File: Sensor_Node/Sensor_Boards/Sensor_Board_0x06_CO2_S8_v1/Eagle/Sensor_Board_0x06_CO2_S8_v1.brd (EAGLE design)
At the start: 55 x 35 mm, 15 parts, among them J1 M04_SMD_90, J3 M03_SMD_90, J4 ARDUINO_ISP, U1 SENSEAIR_S8_SMD, U2 ATMEGA328P_TQFP, Y1 8MHZ

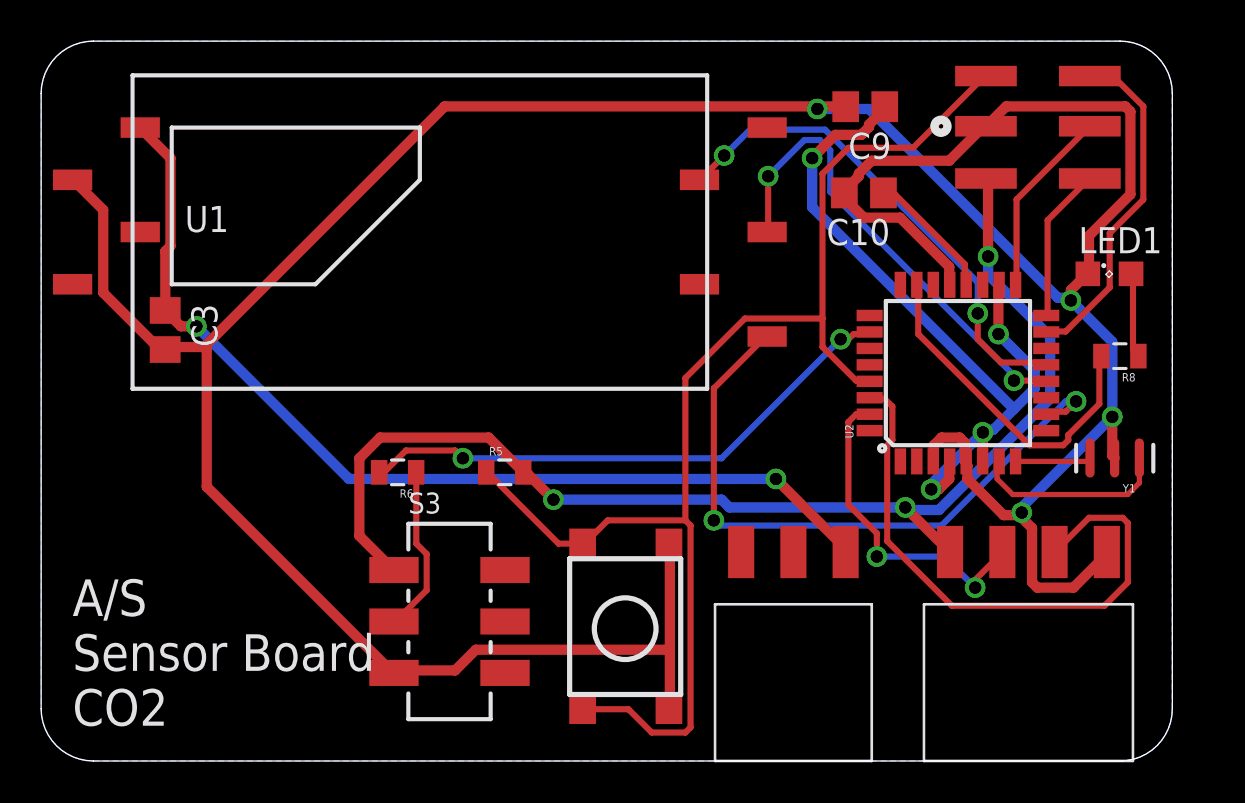
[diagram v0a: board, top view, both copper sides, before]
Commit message: Changes on SensModule CO2 S8
- added poppin programming connector
- moved communication connectors closer together
- turned C3
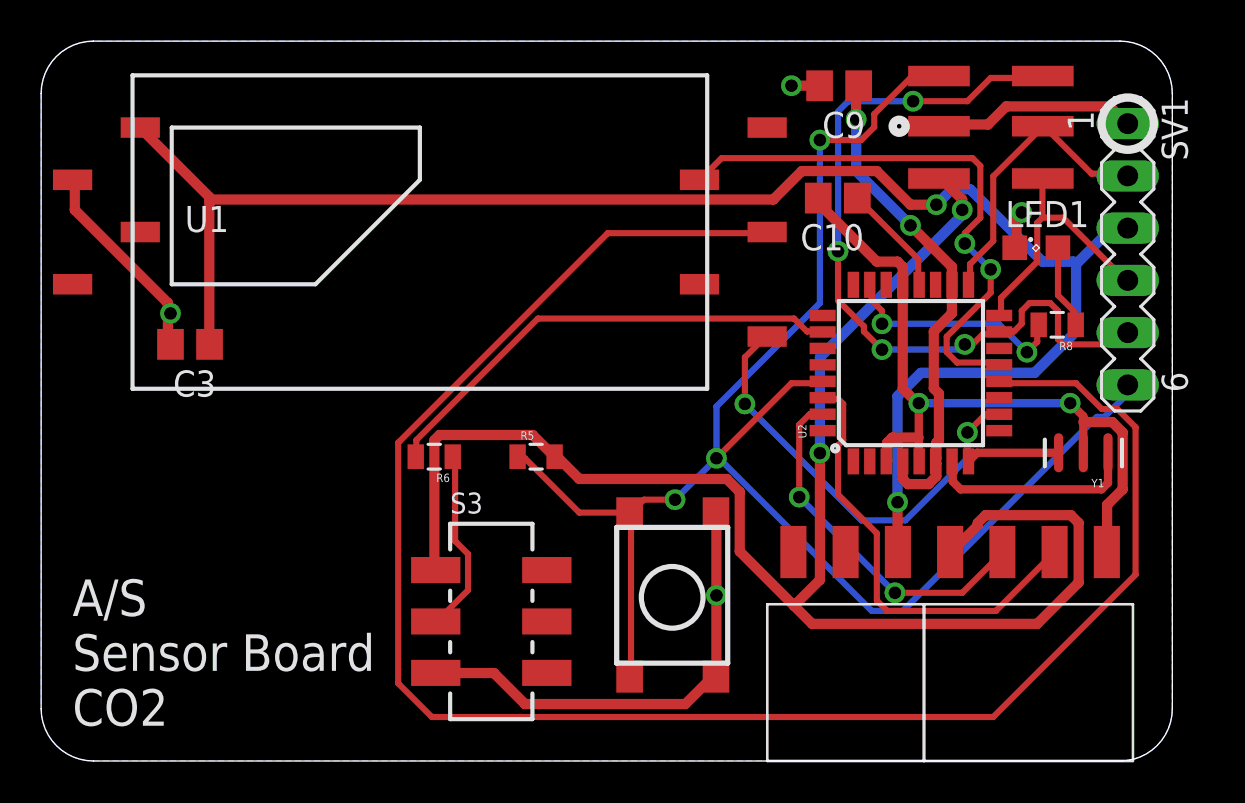
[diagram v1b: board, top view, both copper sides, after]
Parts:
- added SV1: (no value), con-lstb:MA06-1
- moved LED1 3.78 mm to (48.4, 25.0)
- moved R8 3.41 mm to (49.4, 21.2)
- moved S1 2.75 mm to (32.8, 12.0)
- moved J3 2.54 mm to (36.6, 10.2)
- moved U2 2.29 mm to (42.3, 18.9)
- moved J4 2.29 mm to (48.7, 28.3)
- moved S3 2.03 mm to (21.9, 6.78)
- moved R6 1.93 mm to (19.1, 14.8)
- moved R5 1.70 mm to (24.1, 14.8)
- moved C9 1.63 mm to (38.8, 32.8)
- moved Y1 1.55 mm to (50.7, 15.0)
- moved C3 1.39 mm to (7.24, 20.3), turned to 180 degrees
- moved C10 1.30 mm to (38.7, 27.4)
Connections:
- net +5V: now also SV1.3
- net GND: now also SV1.1
- net MISO: now also SV1.4
- net MOSI: now also SV1.5
- net RESET: now also SV1.6
- net SCK: now also SV1.2
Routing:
- net GND: track 170.9 -> 82.3 mm, vias 4 -> 6
- net SENS_TX: track 23.2 -> 88.0 mm, vias 2 -> 0
- net +5V: track 47.7 -> 81.2 mm
- net MOSI: track 16.7 -> 38.3 mm, vias 0 -> 4
- net +3V3: track 59.0 -> 78.9 mm, vias 3 -> 2
- net RESET: track 63.8 -> 79.6 mm, vias 0 -> 3
- net VCC: track 37.3 -> 24.3 mm, vias 4 -> 2
- net SENS_CAL: track 32.0 -> 21.3 mm
- net MCU_RXI: track 28.6 -> 21.6 mm
- net L1: track 16.9 -> 11.4 mm, vias 0 -> 2
- net MISO: track 7.54 -> 12.9 mm
- net SCK: track 9.20 -> 14.3 mm
- net DBG_ENABLE: track 27.0 -> 23.3 mm, vias 2 -> 0
- net SENS_RX: track 24.2 -> 27.9 mm
- net MCU_TXO: track 16.0 -> 17.5 mm
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
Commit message: Changes on all boards
- added capacitor on reset-path
- changed order of pogopin programmer pins

Pulse-Board:
- Deleted input-jumper. Currently one interrupt-pin missing, so print is
not yet routed.
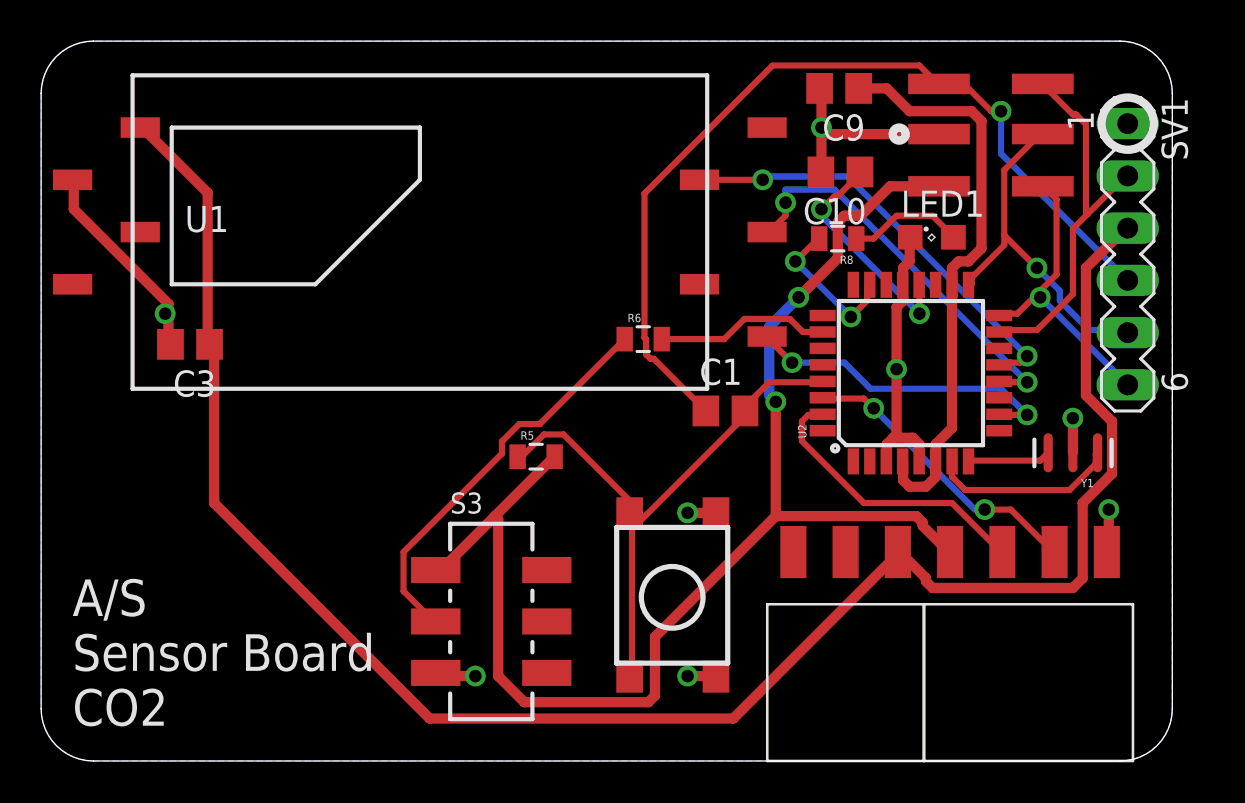
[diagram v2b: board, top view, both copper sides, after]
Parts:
- added C1: 100n, eagle-ltspice:C0805
- moved R6 11.7 mm to (29.3, 20.5), turned to 0 degrees
- moved R8 11.5 mm to (38.7, 25.4)
- moved LED1 5.11 mm to (43.3, 25.5)
- moved C10 1.28 mm to (38.9, 28.6)
- moved Y1 0.51 mm to (50.2, 15.0)
- moved J4 0.38 mm to (48.7, 27.9)
- moved C9 0.13 mm to (38.8, 32.7)
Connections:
- removed net SCL: U2.28
- removed net SDA: U2.27
- new net N$9: C1.2, R5.1, S1.3, S1.4, U2.29
- net MISO: now also SV1.6; no longer SV1.4
- net MOSI: now also SV1.2; no longer SV1.5
- net RESET: now also C1.1, SV1.4; no longer R5.1, S1.3, S1.4, SV1.6, U2.29
- net SCK: now also SV1.5; no longer SV1.2
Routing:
- net SENS_TX: track 88.0 -> 19.5 mm, vias 0 -> 2
- net GND: track 82.3 -> 42.3 mm, vias 6 -> 8
- net RESET: track 79.6 -> 43.6 mm, vias 3 -> 1
- net N$9: track 0.00 -> 28.6 mm
- net MOSI: track 38.3 -> 18.6 mm, vias 4 -> 0
- net DBG_ENABLE: track 23.3 -> 8.49 mm
- net +3V3: track 78.9 -> 66.1 mm
- net N$4: track 9.01 -> 19.5 mm
- net +5V: track 81.2 -> 89.9 mm, vias 2 -> 0
- net MCU_RXI: track 21.6 -> 14.4 mm, vias 0 -> 2
- net SENS_RX: track 27.9 -> 21.2 mm
- net N$15: track 5.45 -> 11.2 mm, vias 0 -> 2
- net SENS_CAL: track 21.3 -> 15.7 mm
- net L1: track 11.4 -> 7.38 mm
- net VCC: track 24.3 -> 28.0 mm, vias 2 -> 0
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
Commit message: Finished some boards.
- Minor changes on all boards except
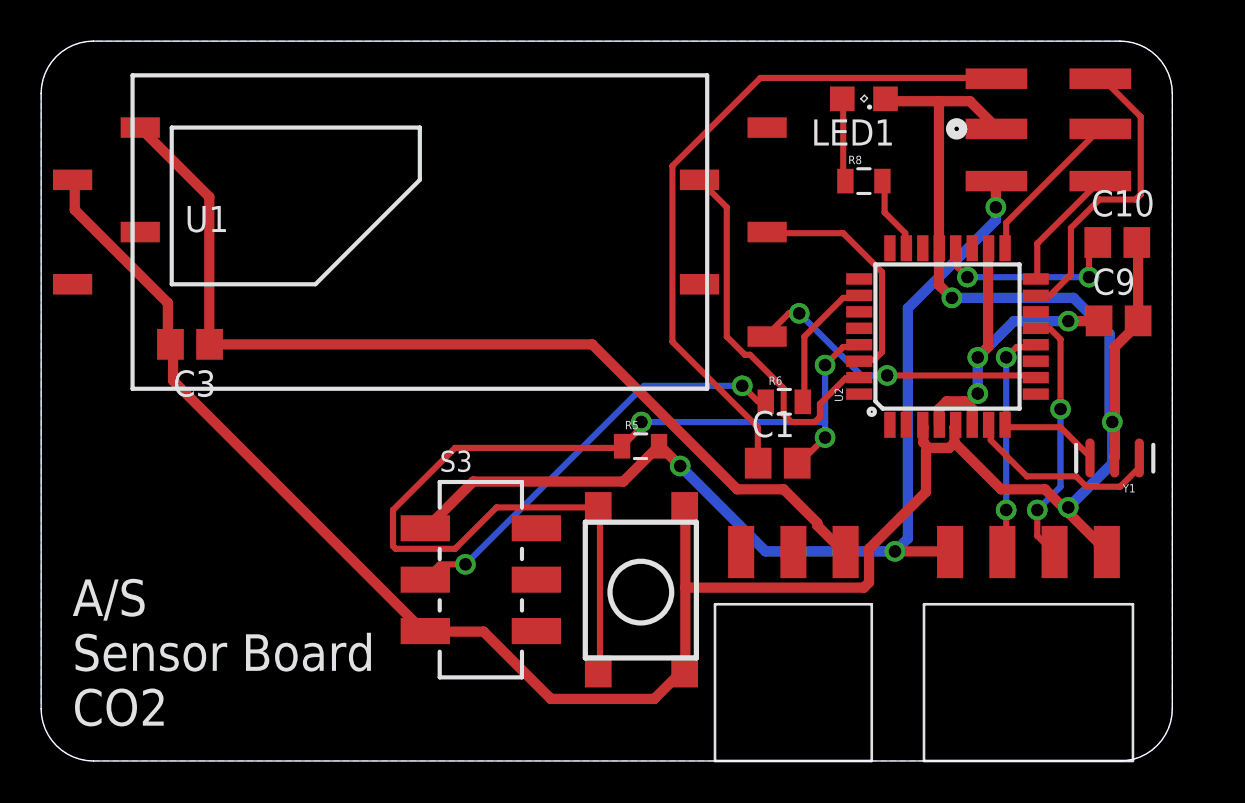
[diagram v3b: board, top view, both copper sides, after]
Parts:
- removed SV1: (no value), con-lstb:MA06-1
- moved C9 17.7 mm to (52.4, 21.4), turned to 0 degrees
- moved C10 13.9 mm to (52.3, 25.2), turned to 0 degrees
- moved R6 7.50 mm to (36.1, 17.5)
- moved LED1 7.50 mm to (40.0, 32.2), turned to 180 degrees
- moved R5 5.11 mm to (29.1, 15.3)
- moved C1 3.59 mm to (35.8, 14.5)
- moved R8 3.07 mm to (40.0, 28.2), turned to 0 degrees
- moved J4 2.81 mm to (51.5, 28.2)
- moved J3 2.54 mm to (34.0, 10.2)
- moved U2 2.51 mm to (44.1, 20.6)
- moved S3 2.09 mm to (21.4, 8.82)
- moved Y1 2.05 mm to (52.2, 14.7)
- moved S1 1.55 mm to (31.3, 12.3)
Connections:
- net +5V: no longer SV1.3
- net GND: no longer SV1.1
- net MCU_RXI: now also U2.13; no longer U2.30
- net MCU_TXO: now also U2.12; no longer U2.31
- net MISO: no longer SV1.6
- net MOSI: no longer SV1.2
- net RESET: no longer SV1.4
- net SCK: no longer SV1.5
- net SENS_RX: now also U2.31; no longer U2.13
- net SENS_TX: now also U2.30; no longer U2.12
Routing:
- net GND: track 42.3 -> 126.4 mm, vias 8 -> 3
- net +5V: track 89.9 -> 47.1 mm
- net N$9: track 28.6 -> 51.1 mm, vias 0 -> 3
- net +3V3: track 66.1 -> 49.3 mm, vias 2 -> 3
- net RESET: track 43.6 -> 33.7 mm, vias 1 -> 0
- net VCC: track 28.0 -> 18.1 mm, vias 0 -> 3
- net SCK: track 17.2 -> 7.71 mm, vias 1 -> 0
- net MISO: track 14.5 -> 6.07 mm, vias 1 -> 0
- net SENS_TX: track 19.5 -> 11.6 mm, vias 2 -> 0
- net L1: track 7.38 -> 3.78 mm, vias 2 -> 0
- net MOSI: track 18.6 -> 15.0 mm
- net SENS_RX: track 21.2 -> 18.3 mm, vias 2 -> 0
- net MCU_TXO: track 14.1 -> 11.3 mm, vias 0 -> 2
- net MCU_RXI: track 14.4 -> 12.6 mm
- net N$15: track 11.2 -> 9.43 mm
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
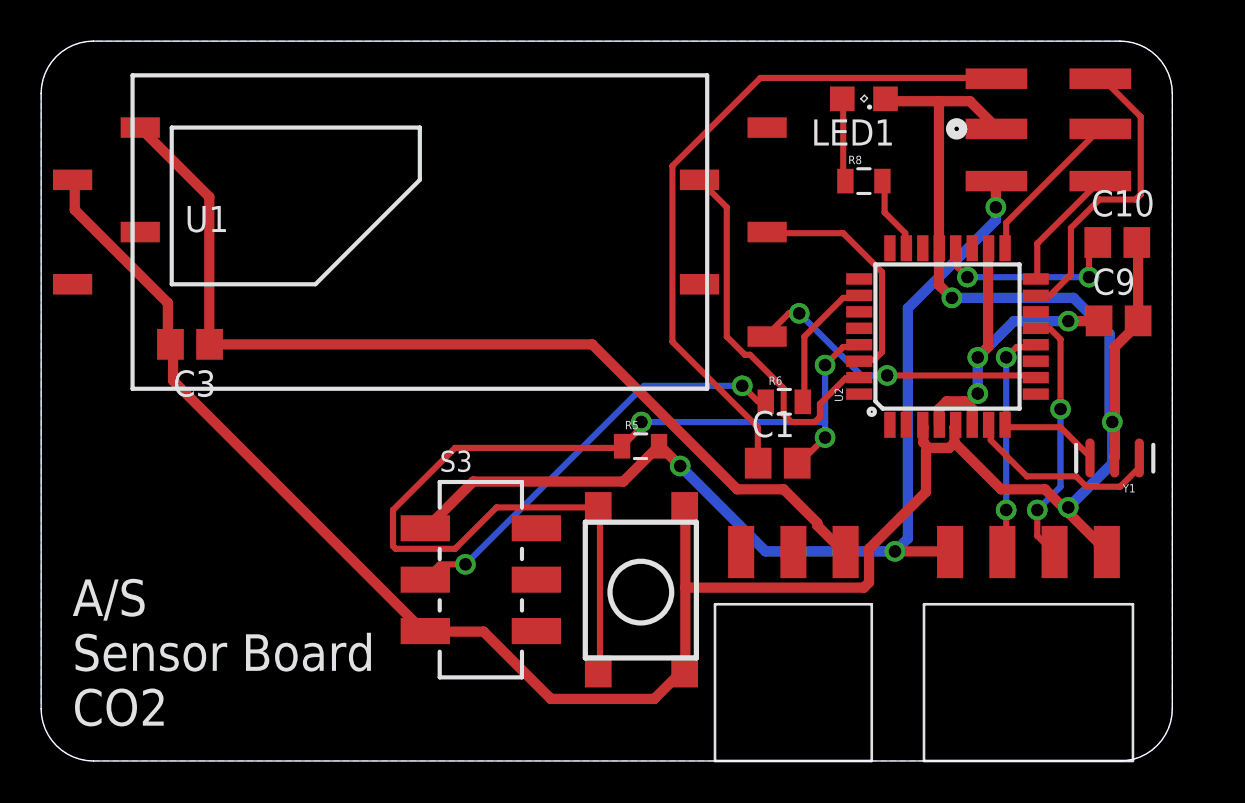
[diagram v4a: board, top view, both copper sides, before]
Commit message: Removed gap between connectors to commBoard, added power jack
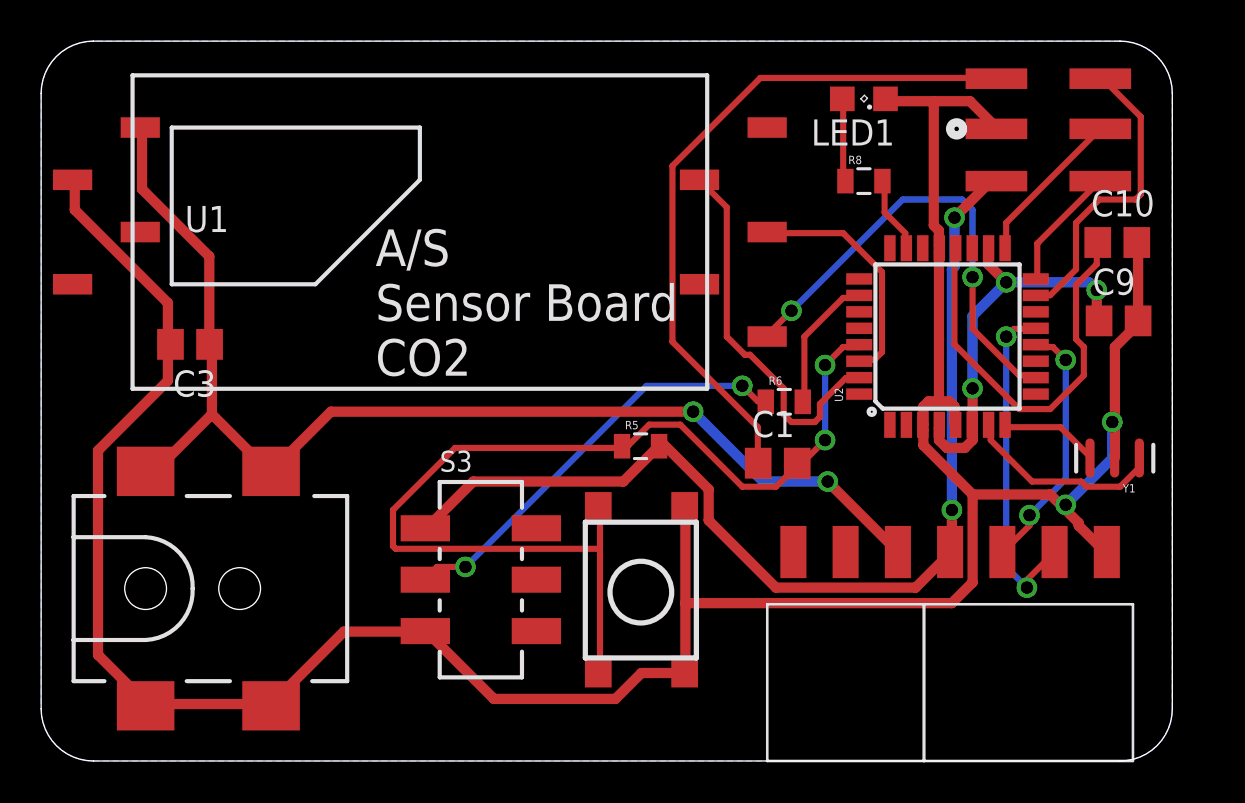
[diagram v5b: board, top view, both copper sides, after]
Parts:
- added J2: 5.5x2.1mm Barrel, wsn:POWER_JACK_SMD
- moved J3 2.54 mm to (36.6, 10.2)
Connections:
- net +5V: now also J2.VIN0, J2.VIN1
- net GND: now also J2.GND, J2.P$4
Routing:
- net GND: track 126.4 -> 139.0 mm, vias 3 -> 2
- net +5V: track 47.1 -> 58.3 mm, vias 0 -> 2
- net N$15: track 9.43 -> 20.0 mm, vias 2 -> 0
- net SENS_CAL: track 14.9 -> 22.8 mm
- net MCU_RXI: track 12.6 -> 16.5 mm
- net +3V3: track 49.3 -> 50.9 mm, vias 3 -> 2
- net MCU_TXO: track 11.3 -> 12.4 mm
- net VCC: track 18.1 -> 19.2 mm
- net N$9: track 51.1 -> 50.8 mm, vias 3 -> 2

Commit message: CO2-Board
- reset path
- some small changes
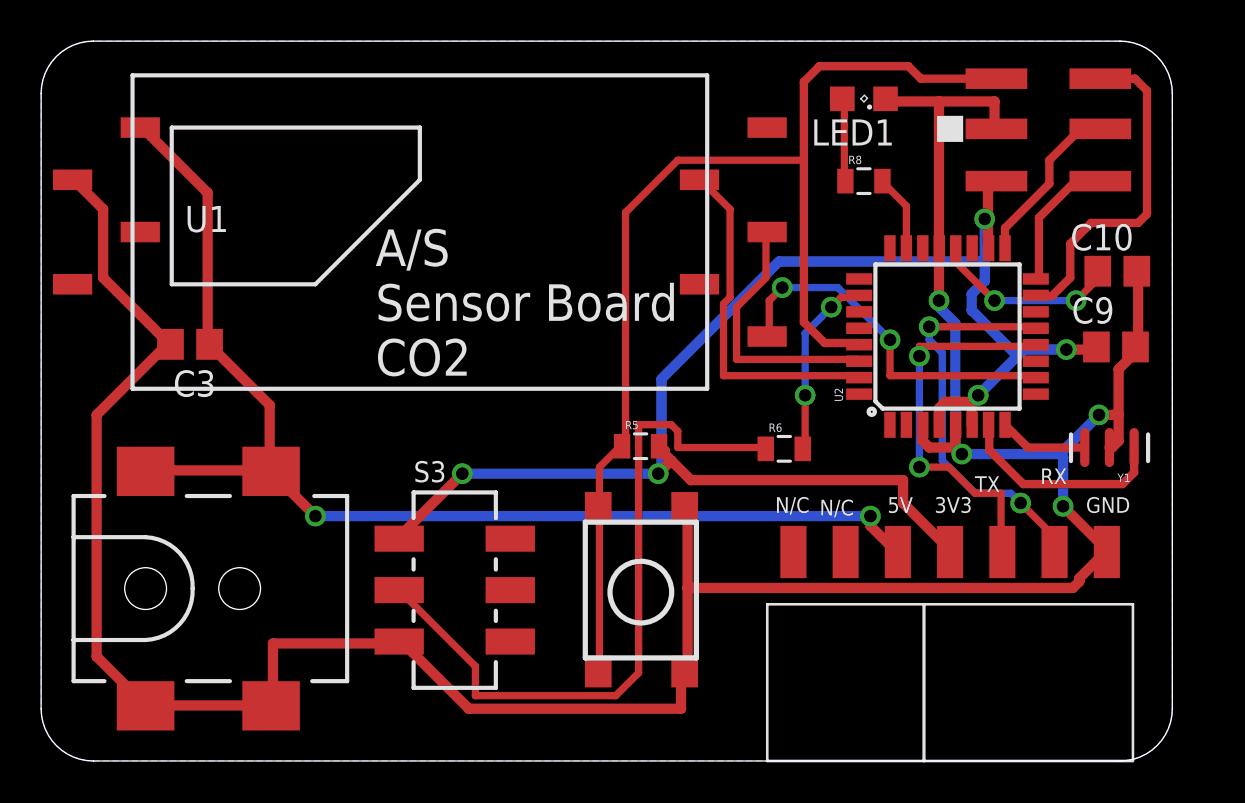
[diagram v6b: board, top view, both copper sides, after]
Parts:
- removed C1: 100n, eagle-ltspice:C0805
- moved R6 2.29 mm to (36.1, 15.2)
- moved C10 1.40 mm to (52.3, 23.8)
- moved S3 1.37 mm to (20.1, 8.31)
- moved C9 1.28 mm to (52.3, 20.1)
- moved Y1 0.57 mm to (51.9, 15.2)
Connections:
- removed net N$9: C1.2, R5.1, S1.3, S1.4, U2.29
- removed net VCC: C9.1, U2.18, U2.4, U2.6
- net +3V3: now also C9.1, U2.18, U2.4, U2.6
- net RESET: now also R5.1, S1.3, S1.4, U2.29; no longer C1.1
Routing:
- net N$9: track 50.8 -> 0.00 mm, vias 2 -> 0
- net +3V3: track 50.9 -> 77.0 mm, vias 2 -> 5
- net RESET: track 33.7 -> 57.4 mm
- net VCC: track 19.2 -> 0.00 mm, vias 3 -> 0
- net N$4: track 20.8 -> 34.2 mm, vias 2 -> 0
- net N$15: track 20.0 -> 9.24 mm, vias 0 -> 2
- net MCU_TXO: track 12.4 -> 19.0 mm
- net SENS_CAL: track 22.8 -> 17.9 mm
- net GND: track 139.0 -> 143.8 mm, vias 2 -> 4
- net MCU_RXI: track 16.5 -> 19.7 mm
- net DBG_ENABLE: track 6.77 -> 9.08 mm, vias 0 -> 2
- net MOSI: track 15.0 -> 16.6 mm
- net SENS_RX: track 18.3 -> 16.9 mm
- net SENS_TX: track 11.6 -> 12.8 mm
- net MISO: track 6.07 -> 6.76 mm
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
